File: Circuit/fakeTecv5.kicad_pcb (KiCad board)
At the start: 2 copper layers, 25.4 x 52.1 mm, 78 parts, among them J1 EXTRA, J11 FET1 3,3, J12 FET2 3,3, J13 FET3 3,3, J14 GPS Pins, J16 Encoder Pads, J37 SCL, J38 JST-SH-4, J39 SDA, J40 3.3V, J41 GND, J42 FET1, J43 FET2, J44 FET3, J45 GND, J46 3.3V, J47 GND, J48 GND, J49 GND, J5 I2C Oled screen, J50 3.3V, J51 GND, J52 GND, J6 FET1 Drain, J7 FET2 Drain, J8 FET3 Drain, J9 JST-PH-2, Q1 AO3400A, Q2 AO3400A, Q3 AO3400A, SW1 Reset, SW2 SW_Push, U1 XB8089D0, U2 HT-RA62, U3 nice!nano v2

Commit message: use alignment hole
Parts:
- U3: footprint faketec:NICE!NANO and pro-micro V2_2 SMD -> faketec:NICE!NANO and pro-micro V2_2 SMD_With_Alignment_Holes
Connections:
- net Net-(J7-Pin_1) renamed /VIBRATION
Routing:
- net +BATT: track 73.3 -> 72.7 mm
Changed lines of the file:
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@@
 	(net 21 "/FET3")
 	(net 22 "/SDA")
-	(net 23 "Net-(J7-Pin_1)")
+	(net 23 "/VIBRATION")
 	(net 24 "/GPSRX")
 	(net 25 "/GPS_GND")
@@
 		(sheetname "/")
 		(sheetfile "fakeTecv5.kicad_sch")
-		(attr through_hole)
+		(attr through_hole exclude_from_bom)
 		(fp_line
 			(start -1.38 -1.38)
@@
 		(embedded_fonts no)
 	)
-	(footprint "faketec:NICE!NANO and pro-micro V2_2 SMD"
+	(footprint "faketec:NICE!NANO and pro-micro V2_2 SMD_With_Alignment_Holes"
 		(layer "F.Cu")
 		(at 111.58298 62.78401 180)
 		(property "Reference" "U3"
-			(at 4.04298 11.16401 180)
+			(at 0 0 0)
 			(layer "F.SilkS")
 			(effects
@@
 		)
 		(property "Value" "nice!nano v2"
-			(at 0 17.472 0)
+			(at -0.9033 17.472 0)
 			(layer "F.Fab")
 			(effects
@@
 			(thermal_bridge_angle 0)
 		)
+		(pad "0" thru_hole circle
+			(at -7.62 -15.24 270)
+			(size 1.2 1.2)
+			(drill 0.762)
+			(layers "*.Cu" "*.Mask")
+			(remove_unused_layers no)
+			(net 2 "GND")
+			(pinfunction "GND")
+			(pintype "passive")
+		)
 		(pad "0" smd rect
 			(at -7.62 -15.24 90)
@@
 			(thermal_bridge_angle 0)
 		)
+		(pad "25" thru_hole circle
+			(at 7.6233 -15.24 90)
+			(size 1.2 1.2)
+			(drill 0.762)
+			(layers "*.Cu" "*.Mask")
+			(remove_unused_layers no)
+			(net 7 "+BATT")
+			(pinfunction "BAT+")
+			(pintype "power_in")
+		)
 		(pad "25" smd rect
 			(at 7.6233 -15.24 90)
@@
 			(layers "B.Cu" "B.Mask" "B.Paste")
 			(roundrect_rratio 0.25)
-			(net 23 "Net-(J7-Pin_1)")
+			(net 23 "/VIBRATION")
 			(pinfunction "D")
 			(pintype "passive")
@@
 			(size 1.5 1.5)
 			(layers "B.Cu" "B.Mask" "B.Paste")
-			(net 23 "Net-(J7-Pin_1)")
+			(net 23 "/VIBRATION")
 			(pinfunction "Pin_1")
 			(pintype "passive")
@@
 	)
 	(segment
-		(start 103.95968 78.02401)
-		(end 103.2 77.26433)
+		(start 103.95968 75.48731)
+		(end 103.96298 75.48401)
 		(width 0.7)
 		(layer "F.Cu")
@@
 	)
 	(segment
-		(start 103.2 76.24699)
-		(end 103.96298 75.48401)
-		(width 0.7)
-		(layer "F.Cu")
-		(net 7)
-	)
-	(segment
 		(start 104.073 77.91399)
 		(end 103.96298 78.02401)
@@
 	)
 	(segment
-		(start 103.2 77.26433)
-		(end 103.2 76.24699)
+		(start 103.95968 78.02401)
+		(end 103.95968 75.48731)
 		(width 0.7)
 		(layer "F.Cu")
@@
 	)
 	(segment
-		(start 120.93 50.08401)
+		(start 120.83298 50.08401)
 		(end 119.20298 50.08401)
 		(width 0.3)

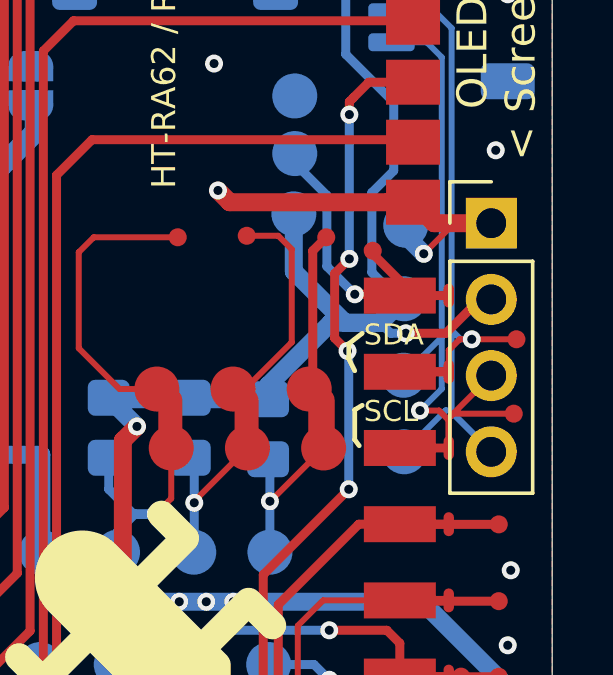
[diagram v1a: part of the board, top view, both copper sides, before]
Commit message: adjust extra testpoint to the side of oled screen
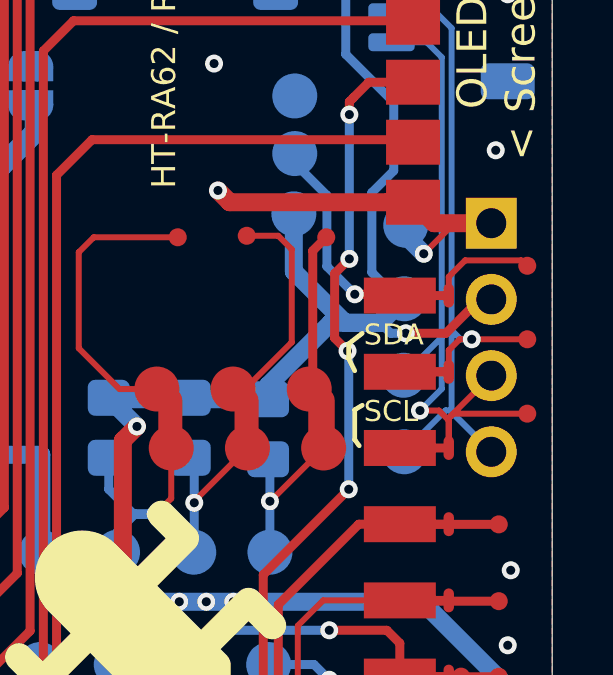
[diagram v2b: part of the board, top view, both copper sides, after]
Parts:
- J5: footprint Connector_PinHeader_2.54mm:PinHeader_1x04_P2.54mm_Vertical -> faketec:OLED_PinHeader_1x04_P2.54mm_Vertical
- moved J23 5.17 mm to (123.5, 46.5)
- moved J25 0.45 mm to (123.5, 51.5)
- moved J24 0.36 mm to (123.5, 49.0)
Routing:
- net /EXTRA: track 7.84 -> 9.34 mm
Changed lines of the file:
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@@
 	(footprint "faketec:TestPoint_Pad_Slim_D0.6mm"
 		(layer "F.Cu")
-		(at 118.3 46.05)
+		(at 123.45 46.55)
 		(descr "SMD pad as test Point, diameter 1.0mm")
 		(tags "test point SMD pad")
@@
 		(embedded_fonts no)
 	)
-	(footprint "Connector_PinHeader_2.54mm:PinHeader_1x04_P2.54mm_Vertical"
+	(footprint "faketec:OLED_PinHeader_1x04_P2.54mm_Vertical"
 		(layer "F.Cu")
 		(at 122.25098 45.13101)
@@
 		(attr through_hole exclude_from_bom)
 		(fp_line
-			(start -1.38 -1.38)
-			(end 0 -1.38)
-			(stroke
-				(width 0.12)
-				(type solid)
-			)
-			(layer "F.SilkS")
-		)
-		(fp_line
-			(start -1.38 0)
-			(end -1.38 -1.38)
-			(stroke
-				(width 0.12)
-				(type solid)
-			)
-			(layer "F.SilkS")
-		)
-		(fp_line
-			(start -1.38 1.27)
-			(end -1.38 9)
-			(stroke
-				(width 0.12)
-				(type solid)
-			)
-			(layer "F.SilkS")
-		)
-		(fp_line
-			(start -1.38 1.27)
-			(end 1.38 1.27)
-			(stroke
-				(width 0.12)
-				(type solid)
-			)
-			(layer "F.SilkS")
-		)
-		(fp_line
-			(start -1.38 9)
-			(end 1.38 9)
-			(stroke
-				(width 0.12)
-				(type solid)
-			)
-			(layer "F.SilkS")
-		)
-		(fp_line
-			(start 1.38 1.27)
-			(end 1.38 9)
-			(stroke
-				(width 0.12)
-				(type solid)
-			)
-			(layer "F.SilkS")
-		)
-		(fp_line
 			(start -1.77 -1.77)
 			(end -1.77 9.39)
@@
 		)
 		(fp_text user "${REFERENCE}"
-			(at 0 3.81 90)
+			(at 4.47 3.98 90)
 			(layer "F.Fab")
 			(effects
@@
 	(footprint "faketec:TestPoint_Pad_Slim_D0.6mm"
 		(layer "F.Cu")
-		(at 123 51.48)
+		(at 123.45 51.48)
 		(descr "SMD pad as test Point, diameter 1.0mm")
 		(tags "test point SMD pad")
@@
 	(footprint "faketec:TestPoint_Pad_Slim_D0.6mm"
 		(layer "F.Cu")
-		(at 123.09 49)
+		(at 123.45 49)
 		(descr "SMD pad as test Point, diameter 1.0mm")
 		(tags "test point SMD pad")
@@
 	)
 	(segment
+		(start 120.98199 51.48)
+		(end 123.42 51.48)
+		(width 0.2)
+		(layer "F.Cu")
+		(net 15)
+	)
+	(segment
 		(start 120.83298 52.62401)
 		(end 120.83298 51.62901)
@@
 	)
 	(segment
-		(start 120.98199 51.48)
-		(end 123 51.48)
-		(width 0.2)
-		(layer "F.Cu")
-		(net 15)
-	)
-	(segment
 		(start 120.83298 51.62901)
 		(end 122.25098 50.21101)
@@
 	)
 	(segment
-		(start 123.09 49)
+		(start 123.53 49)
 		(end 121.6 49)
 		(width 0.2)
@@
 	)
 	(segment
-		(start 119.20298 47.54401)
-		(end 119.20298 47.05298)
-		(width 0.3)
+		(start 120.83298 46.91702)
+		(end 120.83298 47.54401)
+		(width 0.2)
 		(layer "F.Cu")
 		(net 33)
 	)
 	(segment
-		(start 119.20298 47.05298)
-		(end 118.15 46)
-		(width 0.3)
+		(start 123.4 46.52)
+		(end 123.25 46.37)
+		(width 0.2)
+		(layer "F.Cu")
+		(net 33)
+	)
+	(segment
+		(start 123.25 46.37)
+		(end 121.38 46.37)
+		(width 0.2)
+		(layer "F.Cu")
+		(net 33)
+	)
+	(segment
+		(start 121.38 46.37)
+		(end 120.83298 46.91702)
+		(width 0.2)
 		(layer "F.Cu")
 		(net 33)
